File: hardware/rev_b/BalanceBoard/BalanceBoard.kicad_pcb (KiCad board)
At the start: 2 copper layers, 49.5 x 49.5 mm, 90 parts, among them J1 47491-0001-TR425, J2 5103309-1, T1 TestPoints, T10 TestPoints, T11 TestPoints, T12 TestPoints, T13 TestPoints, T14 TestPoints, T15 TestPoints, T16 TestPoints, T17 TestPoints, T18 TestPoints, T19 TestPoints, T2 TestPoints, T20 TestPoints, T21 TestPoints, T22 TestPoints, T23 TestPoints, T24 TestPoints, T25 TestPoints, T26 TestPoints, T27 TestPoints, T28 TestPoints, T29 TestPoints, T3 TestPoints, T30 TestPoints, T31 TestPoints, T32 TestPoints, T33 TestPoints, T34 TestPoints, T35 TestPoints, T36 TestPoints, T37 TestPoints, T38 TestPoints, T39 TestPoints, T4 TestPoints, T40 TestPoints, T41 TestPoints, T42 TestPoints, T43 TestPoints, T44 TestPoints, T45 TestPoints, T46 TestPoints, T47 TestPoints, T48 TestPoints, T5 TestPoints, T6 TestPoints, T7 TestPoints, T8 TestPoints, T9 TestPoints, U1 MPU-6050, U2 FT232RL, U3 C8051F850-A-GU, U4 DRV2605LDGST

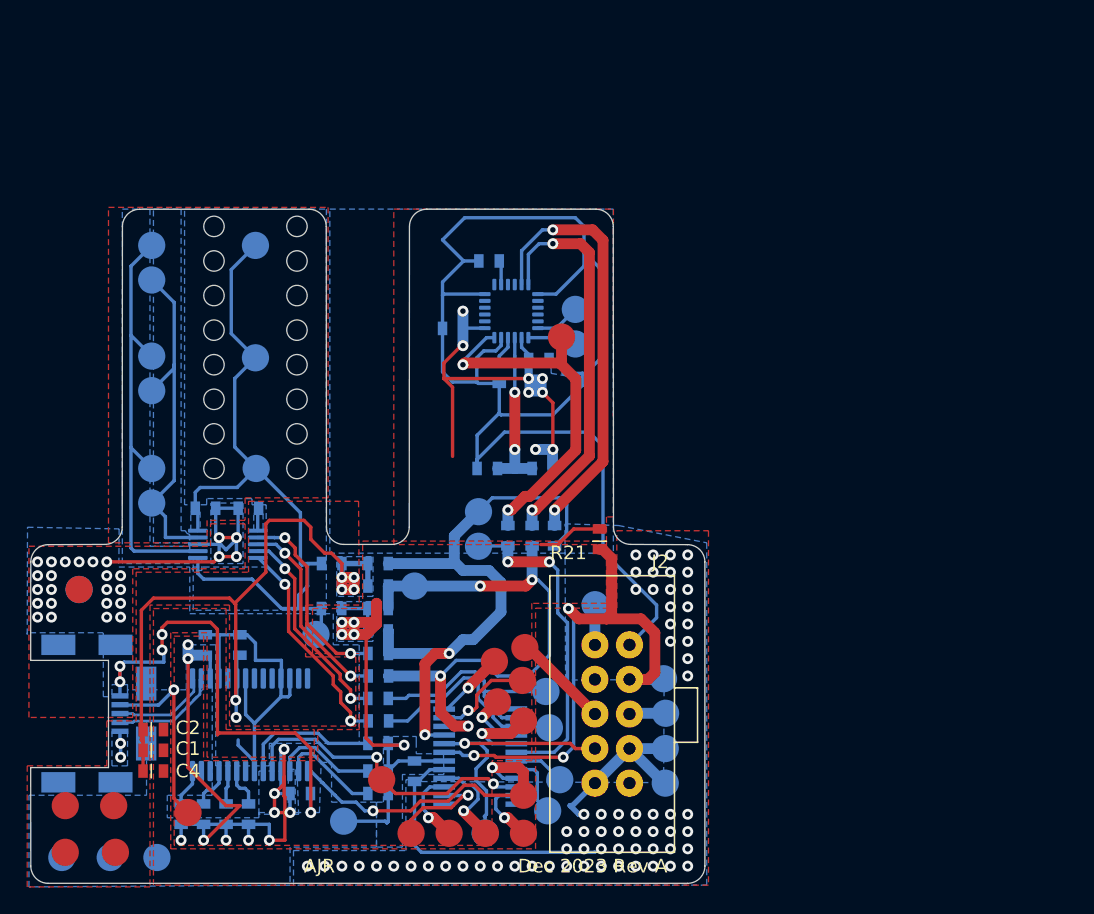
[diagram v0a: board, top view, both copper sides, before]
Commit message: add batt + LDO
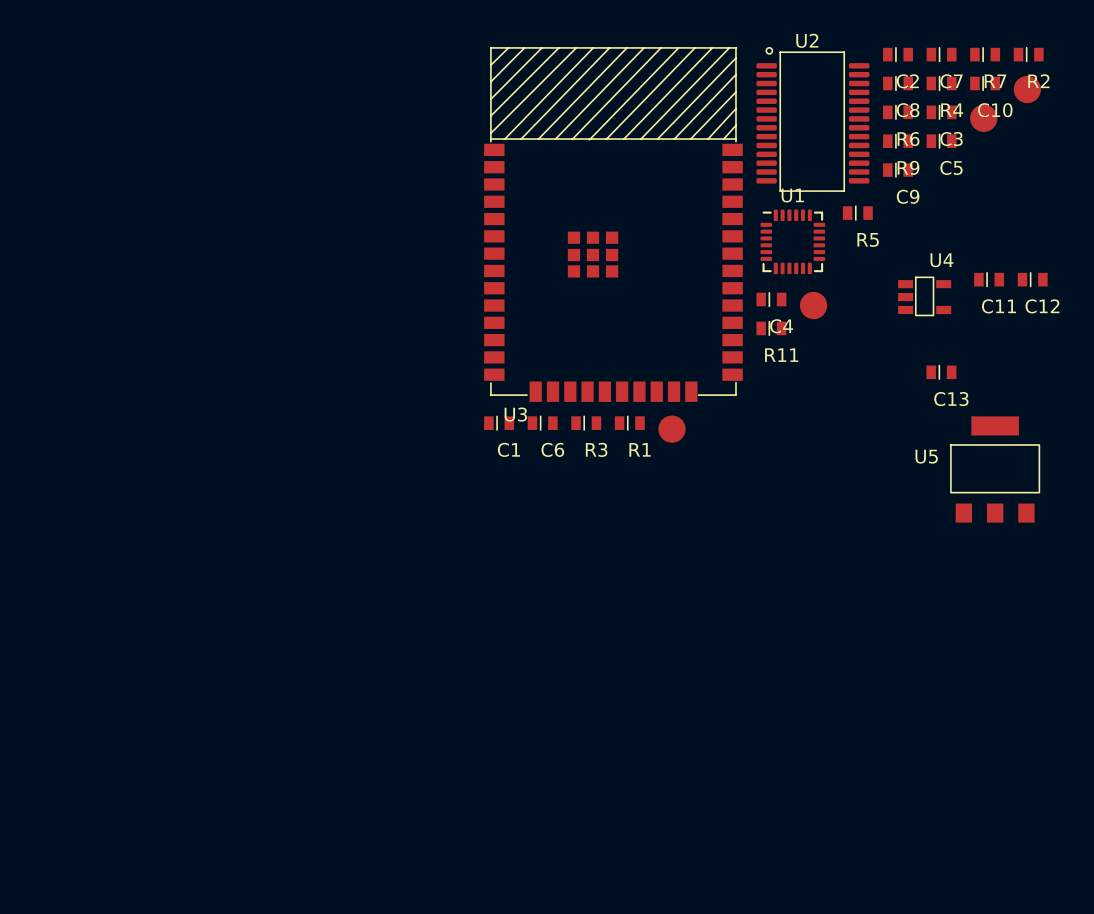
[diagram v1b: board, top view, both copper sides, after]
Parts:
- removed J1: 47491-0001-TR425, receiver:47491-0001-TR425
- removed J2: 5103309-1, receiver:5103309-1
- removed R10, R12, R13, R14, R15, R16, R17, R18, R19, R20, R21, R22, R23, R8: RES_0603, receiver:0603
- removed T10, T11, T12, T13, T14, T15, T16, T17, T18, T19, T2, T20, T21, T22, T23, T24, T25, T26, T27, T28, T29, T3, T30, T31, T32, T33, T34, T35, T36, T37, T38, T39, T4, T40, T41, T42, T43, T44, T45, T46, T47, T48, T5, T6: TestPoints, receiver:TestPoint
- added U5: MIC5239-3.3YS, receiver:MIC5239-3.3YS, F.Cu at (93.9, 146.8)
- C10, C11, C12, C13, C3, C5, C6, C7, C8, C9, R1, R11, R2, R3, R4, R5, R6, R7, R9, T8, T9, U1, U2: moved to F.Cu
- U3: value C8051F850-A-GU -> ESP32-WROOM-32D; footprint receiver:C8051F850-A-GU -> BalanceBoard:ESP32-WROOM-32D; moved to F.Cu
- U4: value DRV2605LDGST -> MCP73831/2; footprint receiver:DRV2605LDGST -> BalanceBoard:MCP738312; moved to F.Cu
- moved T1 77.6 mm to (95.4, 117.8)
- moved R7 76.7 mm to (94.8, 113.1), turned to 0 degrees
- moved R4 75.2 mm to (91.6, 115.2), turned to 0 degrees
- moved C2 73.8 mm to (88.4, 113.1)
- moved R9 68.8 mm to (88.4, 119.5), turned to 0 degrees
- moved C7 67.3 mm to (91.6, 113.1), turned to 0 degrees
- moved R5 65.4 mm to (85.4, 124.8), turned to 0 degrees
- moved C8 65.4 mm to (88.4, 115.2), turned to 0 degrees
- moved R6 62.9 mm to (88.4, 117.4)
- moved U2 61.8 mm to (79.5, 113.9), turned to 0 degrees
- moved C4 57.1 mm to (79.1, 131.1)
- moved C12 57.0 mm to (98.2, 129.6), turned to 0 degrees
- moved C11 55.5 mm to (95.0, 129.6), turned to 0 degrees
- moved C13 55.0 mm to (91.5, 136.4)
- moved U4 50.9 mm to (89.7, 130.0), turned to 0 degrees
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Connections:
- C11 pad 1: Net-(C11-Pad1) -> +5V
- C12 pad 1: +3V3 -> +BATT
- C13 pad 1: Vdrive -> +3V3
- C8 pad 1: +3V3 -> +BATT
- T1 pad 1: Net-(J1-Pad4) -> unconnected-(T1-Pad1)
- U2 pad 17: +3V3 -> unconnected-(U2-Pad17)
- U3 pad 10: /SDA -> unconnected-(U3-Pad10)
- U3 pad 11: Net-(T41-Pad1) -> unconnected-(U3-Pad11)
- U3 pad 12: Net-(T42-Pad1) -> unconnected-(U3-Pad12)
- U3 pad 14: /TRIG -> unconnected-(U3-Pad14)
- U3 pad 15: /EN -> unconnected-(U3-Pad15)
- U3 pad 16: Net-(T40-Pad1) -> unconnected-(U3-Pad16)
- U3 pad 17: Net-(T39-Pad1) -> unconnected-(U3-Pad17)
- U3 pad 18: /INT -> unconnected-(U3-Pad18)
- U3 pad 19: Net-(T38-Pad1) -> unconnected-(U3-Pad19)
- U3 pad 2: Net-(T35-Pad1) -> unconnected-(U3-Pad2)
- U3 pad 20: Net-(T37-Pad1) -> unconnected-(U3-Pad20)
- U3 pad 21: /FT_TO_MCU -> unconnected-(U3-Pad21)
- U3 pad 22: /MCU_TO_FT -> unconnected-(U3-Pad22)
- U3 pad 23: Net-(T36-Pad1) -> unconnected-(U3-Pad23)
- U3 pad 3: Net-(T34-Pad1) -> unconnected-(U3-Pad3)
- U3 pad 4: Net-(T33-Pad1) -> unconnected-(U3-Pad4)
- U3 pad 5: GND -> unconnected-(U3-Pad5)
- U3 pad 6: +3V3 -> unconnected-(U3-Pad6)
- U3 pad 7: /TDI_C2CK -> unconnected-(U3-Pad7)
- U3 pad 8: /TCK_C2D -> unconnected-(U3-Pad8)
- U3 pad 9: /SCL -> unconnected-(U3-Pad9)
- U4 pad 1: Net-(C11-Pad1) -> unconnected-(U4-Pad1)
- U4 pad 2: /DRV_SCL -> GND
- U4 pad 3: /DRV_SDA -> +BATT
- U4 pad 4: /DRV_TRIG -> +5V
- U4 pad 5: /DRV_EN -> unconnected-(U4-Pad5)
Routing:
- net GND: track 217.9 -> 0.00 mm, vias 97 -> 0
- net +3V3: track 134.8 -> 0.00 mm, vias 24 -> 0
- net +5V: track 57.6 -> 0.00 mm, vias 8 -> 0
- net Vdrive: track 55.2 -> 0.00 mm
- net /SDA: track 48.2 -> 0.00 mm, vias 4 -> 0
- net /SCL: track 45.9 -> 0.00 mm, vias 2 -> 0
- net /TDI_C2CK: track 40.7 -> 0.00 mm, vias 3 -> 0
- net /OUT+: track 32.2 -> 0.00 mm
- net /MPU_SCL: track 31.8 -> 0.00 mm, vias 2 -> 0
- net /MPU_SDA: track 29.2 -> 0.00 mm, vias 2 -> 0
- net /MPU_INT: track 27.2 -> 0.00 mm, vias 2 -> 0
- net /OUT-: track 25.7 -> 0.00 mm
- net /FT_TO_MCU: track 24.3 -> 0.00 mm, vias 2 -> 0
- net /INT: track 23.9 -> 0.00 mm, vias 2 -> 0
- net /MCU_TO_FT: track 23.1 -> 0.00 mm, vias 2 -> 0
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- removed copper zone on F.Cu, net (none)
- removed copper zone on B.Cu, net +3V3
- removed copper zone on F.Cu, net +3V3
- removed copper zone on B.Cu, net +5V
- removed copper zone on F.Cu, net +5V
- removed copper zone on B.Cu, net /OUT+
- removed copper zone on B.Cu, net /OUT-
- removed copper zone on B.Cu, net GND
- removed copper zone on F.Cu, net GND
- removed copper zone on B.Cu, net Net-(C11-Pad1)
- removed copper zone on B.Cu, net Vdrive
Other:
- board outline removed
- board text removed: "AJR"
- board text removed: "Dec 2023 Rev A"

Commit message: Update schematic
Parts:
- added C14: CAP_0603, receiver:0603, F.Cu at (152.6, 90.3)
- added C15: CAP_0603, receiver:0603, F.Cu at (152.6, 92.4)
- added C16: CAP_0603, receiver:0603, F.Cu at (149.4, 92.4)
- added C17: CAP_0603, receiver:0603, F.Cu at (139.4, 132.4)
- added C18: CAP_0603, receiver:0603, F.Cu at (136.2, 134.5)
- added C19: CAP_0603, receiver:0603, F.Cu at (136.2, 138.7)
- added C20: CAP_0603, receiver:0603, F.Cu at (142.6, 132.4)
- added C21: CAP_0603, receiver:0603, F.Cu at (132.6, 141.4)
- added C22: CAP_0603, receiver:0603, F.Cu at (129.4, 143.6)
- added C23: CAP_0603, receiver:0603, F.Cu at (129.4, 141.4)
- added C24: CAP_0603, receiver:0603, F.Cu at (129.4, 139.3)
- added J1: 48037-0001, receiver:48037-0001, F.Cu at (205.7, 118.5)
- added R10: RES_0603, receiver:0603, F.Cu at (132.6, 139.3)
- added R12: RES_0603, receiver:0603, F.Cu at (136.2, 132.4)
- added R13: RES_0603, receiver:0603, F.Cu at (136.2, 136.6)
- added R14: RES_0603, receiver:0603, F.Cu at (139.4, 134.5)
- added R8: RES_0603, receiver:0603, F.Cu at (149.4, 90.3)
- added T10: TestPoints, receiver:TestPoint, F.Cu at (140.0, 137.0)
- added T11: TestPoints, receiver:TestPoint, F.Cu at (136.3, 144.3)
- added T12: TestPoints, receiver:TestPoint, F.Cu at (143.2, 134.9)
- added T2: TestPoints, receiver:TestPoint, F.Cu at (140.0, 140.0)
- added T3: TestPoints, receiver:TestPoint, F.Cu at (146.4, 132.8)
- added T4: TestPoints, receiver:TestPoint, F.Cu at (136.5, 141.3)
- added T5: TestPoints, receiver:TestPoint, F.Cu at (143.0, 137.9)
- added T6: TestPoints, receiver:TestPoint, F.Cu at (133.3, 144.0)
- added U6: TB6612FNG, receiver:TB6612FNG, F.Cu at (188.1, 125.4)
- added U7: MIC5239-3.3YS, receiver:MIC5239-3.3YS, F.Cu at (182.9, 142.3)
- U3: moved to B.Cu
- moved U1 121.4 mm to (193.8, 81.2)
- moved U2 116.1 mm to (195.6, 110.9)
- moved U3 103.8 mm to (162.5, 107.4), turned to -90 degrees
- moved U4 99.7 mm to (185.6, 103.1)
- moved U5 84.7 mm to (164.1, 99.2), turned to -90 degrees
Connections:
- R11 pad 1: Net-(R11-Pad1) -> +3V3
- R11 pad 2: +3V3 -> Net-(R11-Pad2)
- R9 pad 1: Net-(R9-Pad1) -> +3V3
- R9 pad 2: +3V3 -> Net-(R9-Pad2)
- T1 pad 1: unconnected-(T1-Pad1) -> /IN1
- U2 pad 10: Net-(R9-Pad1) -> Net-(R9-Pad2)
- U2 pad 6: Net-(R11-Pad1) -> Net-(R11-Pad2)
- U3 pad 1: unconnected-(U3-Pad1) -> GND
- U3 pad 15: unconnected-(U3-Pad15) -> GND
- U3 pad 2: unconnected-(U3-Pad2) -> +3V3
- U3 pad 3: unconnected-(U3-Pad3) -> /EN
- U3 pad 39: unconnected-(U3-Pad39) -> GND
- U4 pad 1: unconnected-(U4-Pad1) -> /STAT
- U4 pad 5: unconnected-(U4-Pad5) -> /PROG

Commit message: Rev B fab out
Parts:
- removed C21, C22, C23, C24: CAP_0603, receiver:0603
- removed R14: RES_0603, receiver:0603
- added M1: MountingHole, receiver:MountingHole, F.Cu at (135.1, 71.5)
- added M2: MountingHole, receiver:MountingHole, F.Cu at (143.1, 63.5)
- added M3: MountingHole, receiver:MountingHole, F.Cu at (101.7, 76.1)
- added M4: MountingHole, receiver:MountingHole, F.Cu at (101.7, 55.8)
- added M5: MountingHole, receiver:MountingHole, F.Cu at (143.1, 71.5)
- added M6: MountingHole, receiver:MountingHole, F.Cu at (101.6, 66.0)
- added T13: TestPoints, receiver:TestPoint, B.Cu at (117.2, 82.2)
- added T14: TestPoints, receiver:TestPoint, F.Cu at (111.0, 60.0)
- added T15: TestPoints, receiver:TestPoint, F.Cu at (104.0, 60.0)
- added T16: TestPoints, receiver:TestPoint, F.Cu at (111.0, 80.0)
- added T17: TestPoints, receiver:TestPoint, F.Cu at (104.0, 80.0)
- added T18: TestPoints, receiver:TestPoint, F.Cu at (111.0, 70.0)
- added T19: TestPoints, receiver:TestPoint, F.Cu at (104.0, 70.0)
- added T20: TestPoints, receiver:TestPoint, B.Cu at (78.0, 103.9)
- added T21: TestPoints, receiver:TestPoint, F.Cu at (61.5, 95.2)
- added U8: ESP32-WROOM-32D, BalanceBoard:ESP32-WROOM-32D, F.Cu at (57.7, 115.4)
- J1: value 48037-0001 -> 61300611121; footprint receiver:48037-0001 -> BalanceBoard:61300611121
- T10, T11, T12, T4, T5, T6, T7, T8, T9: moved to B.Cu
- U1: value MPU-6050 -> MIC5239-3.3YS; footprint Sensor_Motion:InvenSense_QFN-24_4x4mm_P0.5mm -> receiver:MIC5239-3.3YS
- U2: value FT232RL -> MIC5239-3.3YS; footprint receiver:FT232RL -> receiver:MIC5239-3.3YS
- U3: value ESP32-WROOM-32D -> MPU-6050; footprint BalanceBoard:ESP32-WROOM-32D -> Sensor_Motion:InvenSense_QFN-24_4x4mm_P0.5mm; moved to F.Cu
- U4: value MCP73831/2 -> S2B-PH-SM4-TB; footprint BalanceBoard:MCP738312 -> BalanceBoard:S2B-PH-SM4-TB
- U5: value MIC5239-3.3YS -> LP653042; footprint receiver:MIC5239-3.3YS -> BalanceBoard:LP653042; moved to B.Cu
- U6: value TB6612FNG -> MCP73831/2; footprint receiver:TB6612FNG -> BalanceBoard:MCP738312
- U7: value MIC5239-3.3YS -> TB6612FNG; footprint receiver:MIC5239-3.3YS -> receiver:TB6612FNG
- moved T2 117.2 mm to (55.9, 58.4)
- moved T3 112.5 mm to (55.9, 66.0)
- moved U3 111.0 mm to (63.1, 57.9), turned to 0 degrees
- moved J1 102.8 mm to (103.1, 124.0)
- moved U1 100.6 mm to (95.8, 103.9), turned to 180 degrees
- moved C14 98.8 mm to (58.9, 121.7), turned to 180 degrees
- moved U2 98.8 mm to (97.7, 97.2), turned to 90 degrees
- moved U7 94.6 mm to (109.1, 83.2), turned to -90 degrees
- moved T5 92.1 mm to (58.4, 101.6), turned to 180 degrees
- moved C16 91.8 mm to (63.3, 124.2)
- moved R8 88.8 mm to (66.3, 121.7), turned to 180 degrees
- moved T4 88.7 mm to (58.4, 99.1), turned to 180 degrees
- moved T6 84.8 mm to (58.4, 104.1), turned to 180 degrees
- moved T10 84.7 mm to (58.4, 114.3), turned to 180 degrees
- moved T11 82.5 mm to (58.4, 116.8), turned to 180 degrees
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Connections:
- C1 pad 1: +5V -> +BATT
- C10 pad 1: Net-(C10-Pad1) -> +5V
- C11 pad 1: +5V -> +3V3
- C14 pad 1: /EN -> +3V3
- C16 pad 1: +3V3 -> /EN
- C17 pad 1: +BATT -> +3V3
- C18 pad 2: GND -> GND2
- C19 pad 1: +3V3 -> Vdrive
- C19 pad 2: GND -> GND2
- C2 pad 1: +5V -> +BATT
- C20 pad 1: +3V3 -> Vdrive
- C20 pad 2: GND -> GND2
- C4 pad 1: +5V -> +3V3
- C5 pad 1: +3V3 -> Vdrive
- C6 pad 1: +3V3 -> Net-(C6-Pad1)
- C7 pad 1: +5V -> Net-(C7-Pad1)
- C8 pad 1: +BATT -> /MEASURE
- C9 pad 1: Net-(C9-Pad1) -> +3V3
- J1 pad 1: +5V -> GND
- J1 pad 2: /D- -> unconnected-(J1-Pad2)
- J1 pad 3: /D+ -> +5V
- J1 pad 4: GND -> Net-(J1-Pad4)
- J1 pad 5: GND -> Net-(J1-Pad5)
- J1 pad 6: GND -> unconnected-(J1-Pad6)
- R10 pad 1: /STAT -> GND
- R10 pad 2: +3V3 -> /PROG
- R11 pad 1: +3V3 -> GND2
- R11 pad 2: Net-(R11-Pad2) -> GND
- R12 pad 1: GND -> GND2
- R12 pad 2: /PROG -> GND
- R13 pad 1: GND2 -> /EN
- R13 pad 2: GND -> +3V3
- R3 pad 1: Net-(R3-Pad1) -> /MPU_SDA
- R4 pad 1: Net-(R4-Pad1) -> +3V3
- R4 pad 2: +3V3 -> /MPU_SCL
- R5 pad 1: Net-(R5-Pad1) -> /TXD0
- R5 pad 2: +3V3 -> Net-(J1-Pad5)
- R6 pad 1: Net-(R6-Pad1) -> /RXD0
- R6 pad 2: +3V3 -> Net-(J1-Pad4)
- R7 pad 1: Net-(R7-Pad1) -> +BATT
- R7 pad 2: +3V3 -> /MEASURE
- R8 pad 1: /EN -> /MEASURE
- R8 pad 2: +3V3 -> GND
- R9 pad 1: +3V3 -> /STAT
- R9 pad 2: Net-(R9-Pad2) -> +3V3
- T1 pad 1: /IN1 -> /MPU_INT
- T10 pad 1: Net-(U6-Pad5) -> /PWMB
- T11 pad 1: Net-(U6-Pad1) -> Net-(T11-Pad1)
- T12 pad 1: Net-(U6-Pad5) -> /BO1
- T2 pad 1: /IN2 -> Net-(T2-Pad1)
- T3 pad 1: /PWM -> Net-(T3-Pad1)
- T4 pad 1: Net-(U6-Pad1) -> /STBY
- T5 pad 1: Net-(U6-Pad5) -> /AIN1
- T6 pad 1: Net-(U6-Pad1) -> /AIN2
- T7 pad 1: /MPU_INT -> /PWMA
- T8 pad 1: Net-(T8-Pad1) -> /BIN1
- T9 pad 1: Net-(T9-Pad1) -> /BIN2
- U1 pad 1: GND -> +BATT
- U1 pad 2: unconnected-(U1-Pad2) -> GND
- U1 pad 3: unconnected-(U1-Pad3) -> +3V3
- U1 pad 4: unconnected-(U1-Pad4) -> GND
- U2 pad 1: /FT_TO_MCU -> +BATT
- U2 pad 2: Net-(R6-Pad1) -> GND
- U2 pad 3: Net-(R3-Pad1) -> Vdrive
- U2 pad 4: +3V3 -> GND
- U3 pad 10: unconnected-(U3-Pad10) -> Net-(C6-Pad1)
- U3 pad 11: unconnected-(U3-Pad11) -> GND
- U3 pad 12: unconnected-(U3-Pad12) -> /MPU_INT
- U3 pad 13: unconnected-(U3-Pad13) -> +3V3
- U3 pad 15: GND -> unconnected-(U3-Pad15)
- U3 pad 18: unconnected-(U3-Pad18) -> GND
- U3 pad 2: +3V3 -> unconnected-(U3-Pad2)
- U3 pad 20: unconnected-(U3-Pad20) -> Net-(C7-Pad1)
- U3 pad 23: unconnected-(U3-Pad23) -> /MPU_SCL
- U3 pad 24: unconnected-(U3-Pad24) -> /MPU_SDA
- U3 pad 3: /EN -> unconnected-(U3-Pad3)
- U3 pad 6: unconnected-(U3-Pad6) -> Net-(T2-Pad1)
- U3 pad 7: unconnected-(U3-Pad7) -> Net-(T3-Pad1)
- U3 pad 8: unconnected-(U3-Pad8) -> +3V3
- U3 pad 9: unconnected-(U3-Pad9) -> /MPU_AD0
- U4 pad 1: /STAT -> GND
- U4 pad 2: GND -> +BATT
- U4 pad 3: +BATT -> unconnected-(U4-Pad3)
- U4 pad 4: +5V -> unconnected-(U4-Pad4)
- U5 pad 1: +BATT -> unconnected-(U5-Pad1)
- U5 pad 2: GND -> unconnected-(U5-Pad2)
- U6 pad 1: Net-(U6-Pad1) -> /STAT
- U6 pad 2: Net-(U6-Pad1) -> GND
- U6 pad 3: GND2 -> +BATT
- U6 pad 4: GND2 -> +5V
- U6 pad 5: Net-(U6-Pad5) -> /PROG
- U7 pad 1: +BATT -> /AO1
- U7 pad 2: GND -> /AO1
- U7 pad 3: Vdrive -> GND2
- U7 pad 4: GND -> GND2
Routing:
- net GND: track 0.00 -> 315.6 mm, vias 0 -> 75
- net +3V3: track 0.00 -> 192.1 mm, vias 0 -> 39
- net +BATT: track 0.00 -> 123.8 mm, vias 0 -> 2
- net /MPU_SCL: track 0.00 -> 96.2 mm, vias 0 -> 5
- net /MPU_SDA: track 0.00 -> 92.6 mm, vias 0 -> 5
- net /AIN1: track 0.00 -> 87.9 mm, vias 0 -> 3
- net /AIN2: track 0.00 -> 83.3 mm, vias 0 -> 3
- net /STAT: track 0.00 -> 78.8 mm, vias 0 -> 2
- net /PWMA: track 0.00 -> 74.1 mm, vias 0 -> 3
- net /BIN2: track 0.00 -> 61.3 mm, vias 0 -> 2
- net /BIN1: track 0.00 -> 61.1 mm, vias 0 -> 3
- net /PWMB: track 0.00 -> 60.6 mm, vias 0 -> 2
- net /STBY: track 0.00 -> 60.5 mm, vias 0 -> 2
- net /MT: track 0.00 -> 55.0 mm
- net /RXD0: track 0.00 -> 47.0 mm, vias 0 -> 2
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- added copper zone on B.Cu, net +3V3
- added copper zone on F.Cu, net +3V3
- added copper zone on F.Cu, net +BATT
- added copper zone on F.Cu, net /AO1
- added copper zone on F.Cu, net /AO2
- added copper zone on B.Cu, net /BO1
- added copper zone on F.Cu, net /BO1
- added copper zone on B.Cu, net /BO2
- added copper zone on F.Cu, net /BO2
- added copper zone on B.Cu, net /MT
- added copper zone on B.Cu, net GND
- added copper zone on F.Cu, net GND
- added copper zone on F.Cu, net GND2
- added copper zone on B.Cu, net Vdrive
- added copper zone on F.Cu, net Vdrive
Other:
- board outline added: 70 x 80 mm
- board text added: "+"
- board text added: "-"
- board text added: "AIN1"
- board text added: "AIN2"
- board text added: "Ashley J. Robinson"
- board text added: "BIN1"
- board text added: "BIN2"
- board text added: "GND"
- board text added: "PWMA"
- board text added: "PWMB"
- board text added: "RevB June 2024"
- board text added: "STBY"
